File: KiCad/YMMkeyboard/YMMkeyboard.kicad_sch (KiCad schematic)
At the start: 65 parts, among them J2 Conn_01x09, J3 Conn_01x09, SW10 SW_Push, SW11 SW_Push, SW12 SW_Push, SW13 SW_Push, SW14 SW_Push, SW15 SW_Push, SW16 SW_Push, SW17 SW_Push, SW18 SW_Push, SW19 SW_Push, SW2 SW_Push, SW20 SW_Push, SW21 SW_Push, SW22 SW_Push, SW23 SW_Push, SW24 SW_Push, SW25 SW_Push, SW26 SW_Push, SW27 SW_Push, SW28 SW_Push, SW29 SW_Push, SW3 SW_Push, SW30 SW_Push, SW31 SW_Push, SW32 RotaryEncoder_Switch, SW4 SW_Push, SW5 SW_Push, SW6 SW_Push, SW7 SW_Push, SW8 SW_Push, SW9 SW_Push, U2 RP2040-Zero

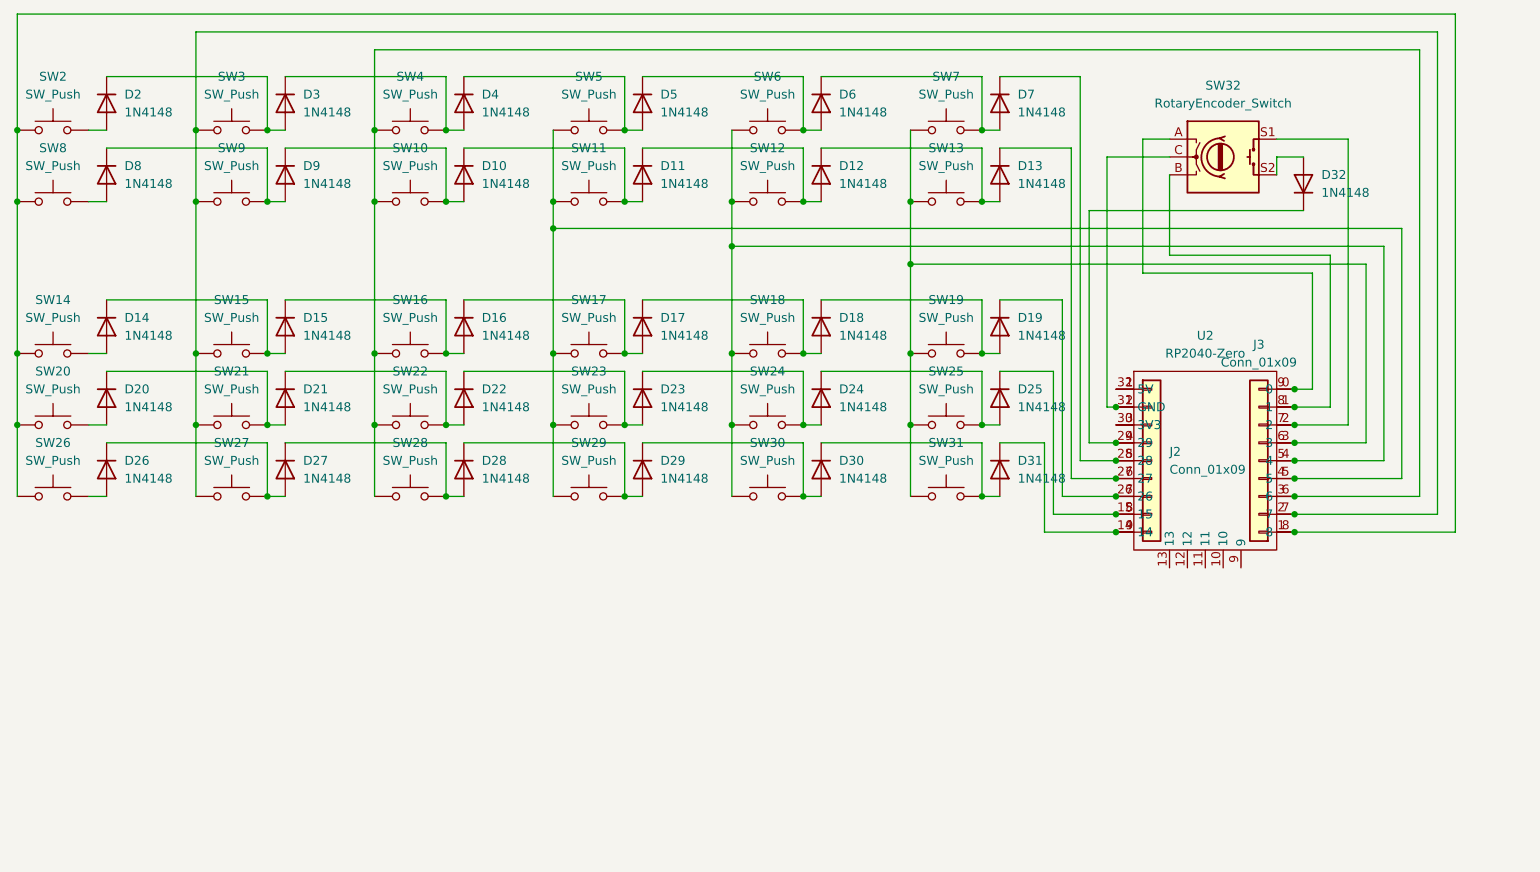
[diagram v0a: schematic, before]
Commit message: キーボードの設計ミスを変更 原因:ダイオードを直列に配置した結果電圧降下した
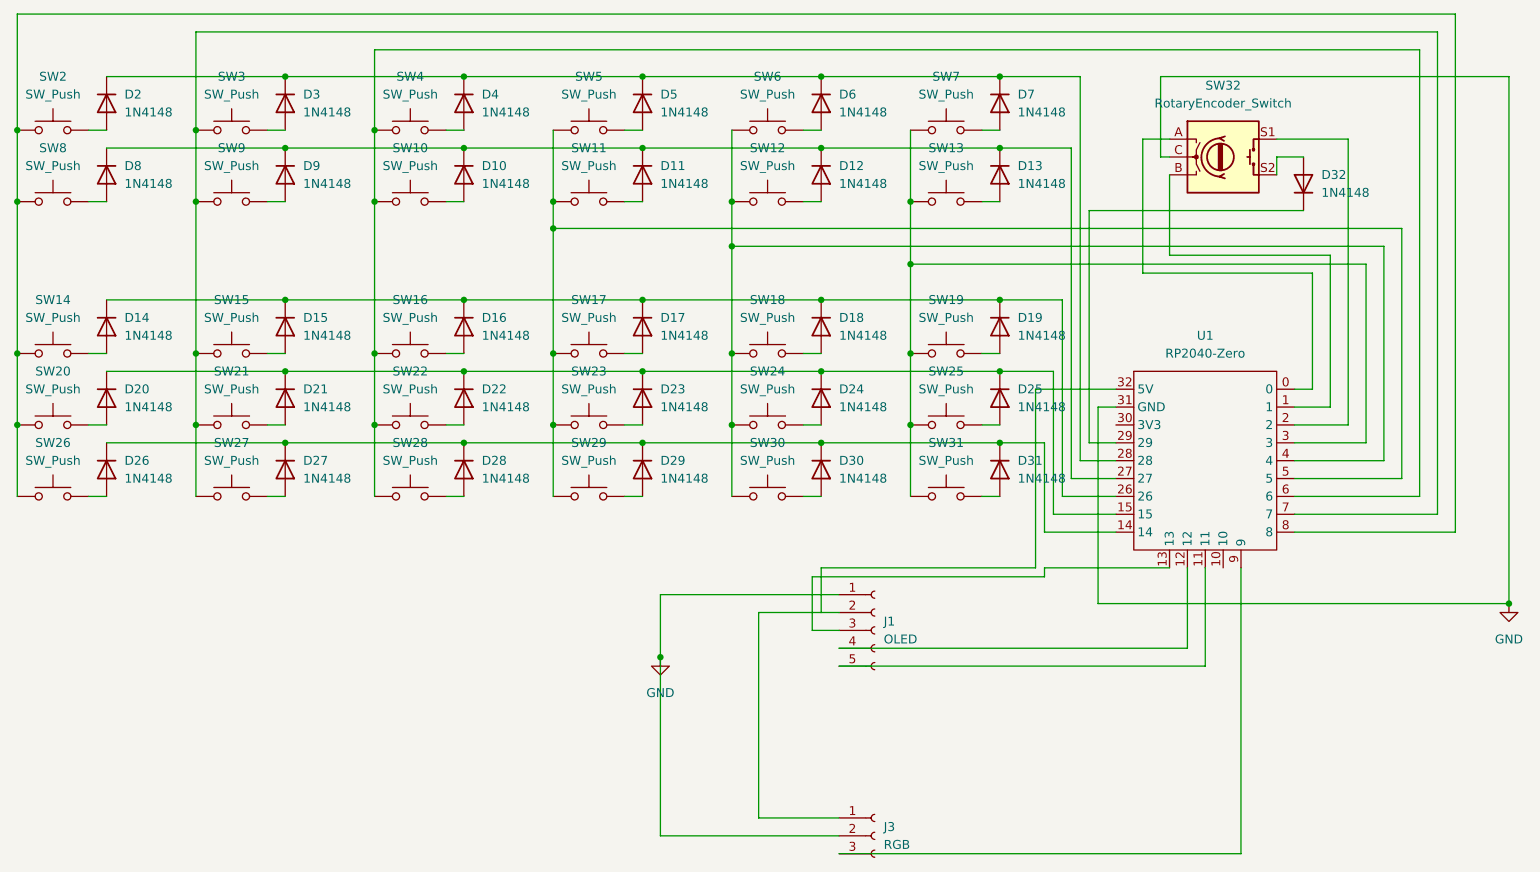
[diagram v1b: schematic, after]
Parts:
- removed J2, J3: Conn_01x09, Connector_PinSocket_2.54mm:PinSocket_1x10_P2.54mm_Vertical, symbol Connector_Generic:Conn_01x09
- removed U2: RP2040-Zero, symbol isw-mcu:RP2040-Zero
- added J1: OLED, symbol Connector:Conn_01x05_Socket
- added J3: RGB, symbol Connector:Conn_01x03_Socket
- added U1: RP2040-Zero, symbol isw-mcu:RP2040-Zero
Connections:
- net at SW13.1, SW19.1, SW25.1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: now also U1.3
- net at D19.2 (A), SW19.2: no longer D18.1 (K)
- net at D27.2 (A), SW27.2: no longer D26.1 (K)
- net at D25.2 (A), SW25.2: no longer D24.1 (K)
- net at SW32.A: now also U1.0
- net at SW32.B: now also U1.1
- net GND: now reaches SW32.C
- net GND: now also J1.1 (Pin_1), J3.2 (Pin_2), U1.31 (GND)
- net at SW32.S1: now also U1.2
- net at D7.2 (A), SW7.2: no longer D6.1 (K)
- net at D30.2 (A), SW30.2: no longer D29.1 (K)
- net at D29.2 (A), SW29.2: no longer D28.1 (K)
- net at D31.2 (A), SW31.2: no longer D30.1 (K)
- net at SW11.1, SW17.1, SW23.1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: now also U1.5
- net at D11.2 (A), SW11.2: no longer D10.1 (K)
- net at D32.1 (K): now also U1.29
- net at D7.1 (K): now also D2.1 (K), D3.1 (K), D4.1 (K), D5.1 (K), D6.1 (K), U1.28
- net at D6.2 (A), SW6.2: no longer D5.1 (K)
- net at D5.2 (A), SW5.2: no longer D4.1 (K)
- net at D10.2 (A), SW10.2: no longer D9.1 (K)
- net at D9.2 (A), SW9.2: no longer D8.1 (K)
- net at D31.1 (K): now also D26.1 (K), D27.1 (K), D28.1 (K), D29.1 (K), D30.1 (K), U1.14
- net at SW10.1, SW16.1, SW22.1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: now also U1.6
- net at D4.2 (A), SW4.2: no longer D3.1 (K)
- net at D23.2 (A), SW23.2: no longer D22.1 (K)
- net at SW15.1, SW21.1, SW27.1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: now also U1.7
- net at D3.2 (A), SW3.2: no longer D2.1 (K)
- net at SW14.1, SW2.1, SW20.1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: now also U1.8
- net at D13.1 (K): now also D10.1 (K), D11.1 (K), D12.1 (K), D8.1 (K), D9.1 (K), U1.27
- net at D13.2 (A), SW13.2: no longer D12.1 (K)
- net at D16.2 (A), SW16.2: no longer D15.1 (K)
- net at D21.2 (A), SW21.2: no longer D20.1 (K)
- net at D24.2 (A), SW24.2: no longer D23.1 (K)
- net at SW12.1, SW18.1, SW24.1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: now also U1.4
- net at D18.2 (A), SW18.2: no longer D17.1 (K)
- net at D22.2 (A), SW22.2: no longer D21.1 (K)
- net at D15.2 (A), SW15.2: no longer D14.1 (K)
- net at D12.2 (A), SW12.2: no longer D11.1 (K)
- net at D19.1 (K): now also D14.1 (K), D15.1 (K), D16.1 (K), D17.1 (K), D18.1 (K), U1.26
- net at D25.1 (K): now also D20.1 (K), D21.1 (K), D22.1 (K), D23.1 (K), D24.1 (K), U1.15
- net at D17.2 (A), SW17.2: no longer D16.1 (K)
- net at D28.2 (A), SW28.2: no longer D27.1 (K)
- new net: J1.5 (Pin_5), U1.11
- new net: J1.4 (Pin_4), U1.12
- new net: J1.3 (Pin_3), U1.13
- new net: J3.3 (Pin_3), U1.9
- new net: J1.2 (Pin_2), J3.1 (Pin_1)

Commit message: 2号機発注データ
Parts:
- J1: footprint (none) -> Connector_PinSocket_2.54mm:PinSocket_1x05_P2.54mm_Vertical
- J3: footprint (none) -> Connector_PinSocket_2.54mm:PinSocket_1x03_P2.54mm_Vertical
- U1: footprint (none) -> RP2040-ZeroSocket:RP2040-ZeroSocket
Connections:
- net at U1.32 (5V): now also J1.2 (Pin_2), J3.1 (Pin_1)
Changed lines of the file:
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@@
 	)
 	(junction
+		(at 160.02 125.73)
+		(diameter 0)
+		(color 0 0 0 0)
+	)
+	(junction
 		(at 109.22 59.69)
 		(diameter 0)
@@
 	(wire
 		(pts
+			(xy 160.02 125.73) (xy 162.56 125.73)
+		)
+		(stroke
+			(width 0)
+			(type default)
+		)
+	)
+	(wire
+		(pts
 			(xy 55.88 109.22) (xy 58.42 109.22)
 		)
@@
 	(wire
 		(pts
-			(xy 151.13 125.73) (xy 162.56 125.73)
+			(xy 151.13 125.73) (xy 160.02 125.73)
 		)
 		(stroke
@@
 			)
 		)
-		(property "Footprint" ""
+		(property "Footprint" "RP2040-ZeroSocket:RP2040-ZeroSocket"
 			(at 214.63 88.9 0)
 			(effects
@@
 			)
 		)
-		(property "Footprint" ""
+		(property "Footprint" "Connector_PinSocket_2.54mm:PinSocket_1x05_P2.54mm_Vertical"
 			(at 167.64 128.27 0)
 			(effects
@@
 			)
 		)
-		(property "Footprint" ""
+		(property "Footprint" "Connector_PinSocket_2.54mm:PinSocket_1x03_P2.54mm_Vertical"
 			(at 167.64 157.48 0)
 			(effects
